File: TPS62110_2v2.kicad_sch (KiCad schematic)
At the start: 13 parts, among them U2901 TPS62110RSAR

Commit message: Schematic Changes
Added Manufacturer/MPN/Description Fields to parts
Added libraries to project
Modified FMC schematic to use new symbol
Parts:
- C2901: Manufacturer (none) -> Murata; Manufacturer Part Number (none) -> GRM188R61E105KA12D
- C2902, C2903: Manufacturer (none) -> Murata; Manufacturer Part Number (none) -> GRM31CR61E226KE15L
- C2904: Manufacturer (none) -> Murata; Manufacturer Part Number (none) -> GRM1885C1H100JA01D
- C2905: Manufacturer (none) -> Murata; Manufacturer Part Number (none) -> GRM31CR61A476ME15L
- FB2901: Manufacturer (none) -> Würth; Manufacturer Part Number (none) -> 742792040
- L2901: Manufacturer (none) -> Würth; Manufacturer Part Number (none) -> 74477710
- R2901, R2902: Manufacturer (none) -> YAGEO; Manufacturer Part Number (none) -> RC0603FR-0711K5L
- R2903, R2904, R2905: Manufacturer (none) -> YAGEO; Manufacturer Part Number (none) -> RC0603FR-07422KL
- U2901: Manufacturer (none) -> Texas Instruments; Manufacturer Part Number (none) -> TPS62110RSAR

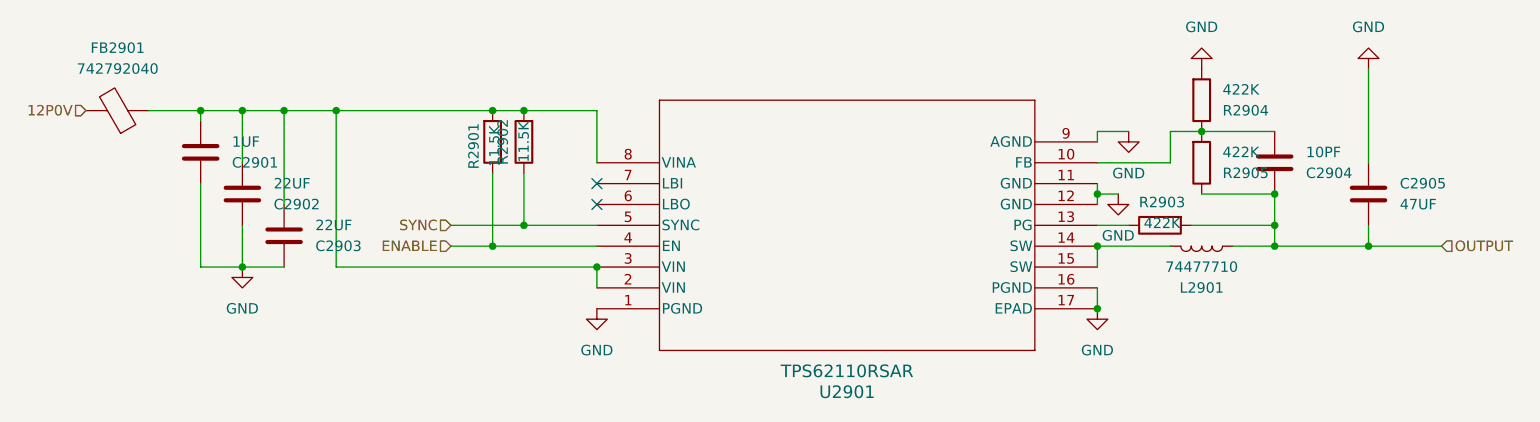
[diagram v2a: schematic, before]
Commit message: Schematics update
Cleaned up RF ADC and front end sections.
Verified that changes did not changes anything about the layout.
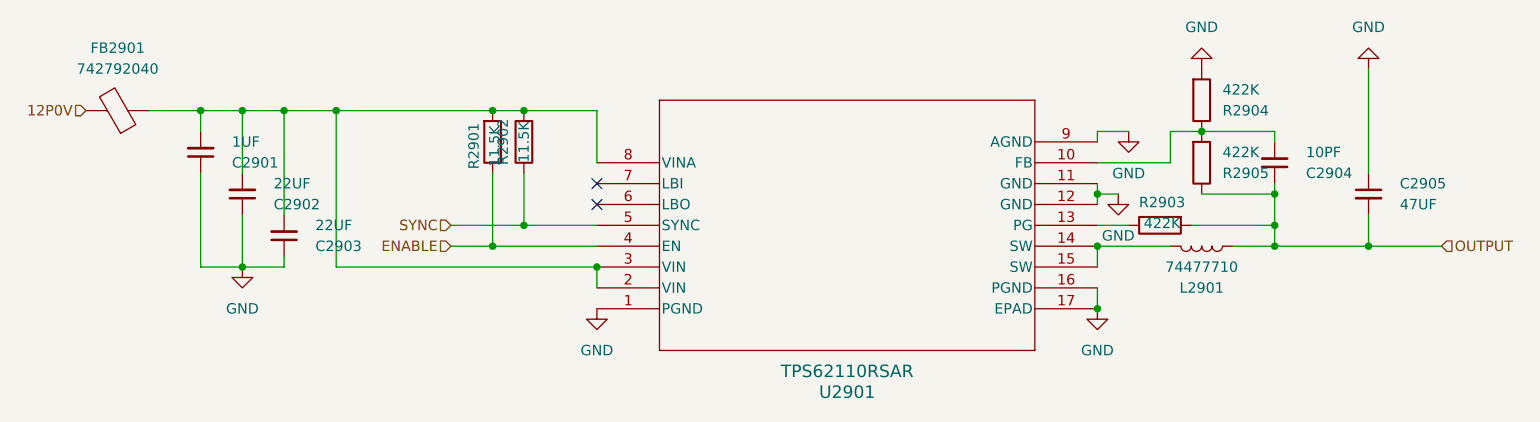
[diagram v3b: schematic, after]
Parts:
- C2901, C2902, C2903, C2904, C2905: symbol Device:C -> Device:C_Small
